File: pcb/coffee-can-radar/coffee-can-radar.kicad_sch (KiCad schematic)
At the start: 23 parts

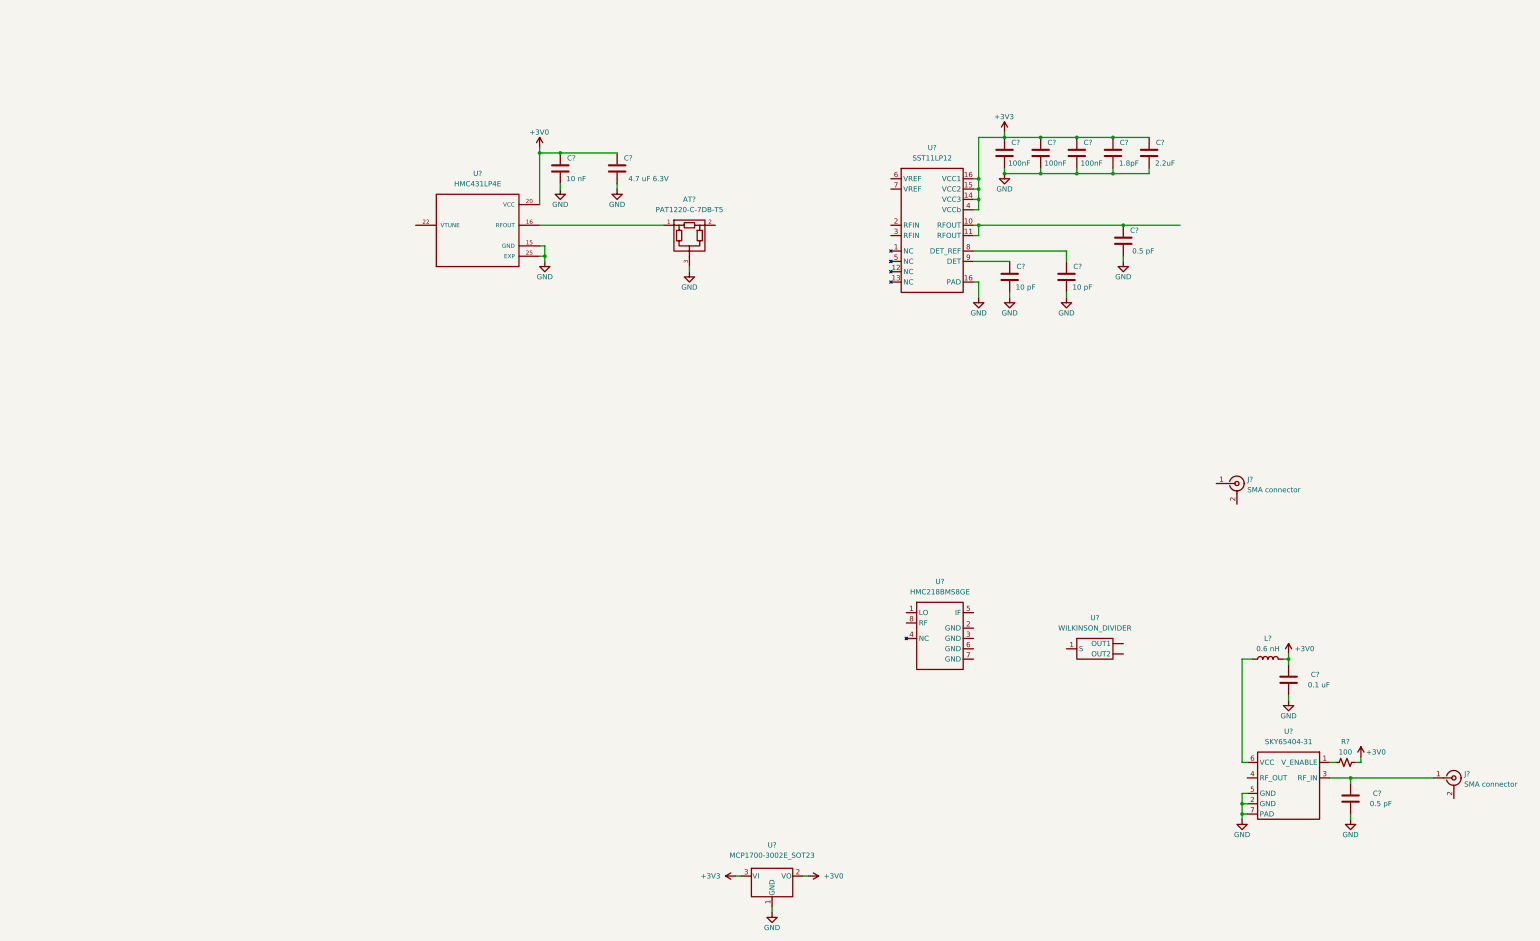
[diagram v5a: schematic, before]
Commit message: Finish RF, add supplies
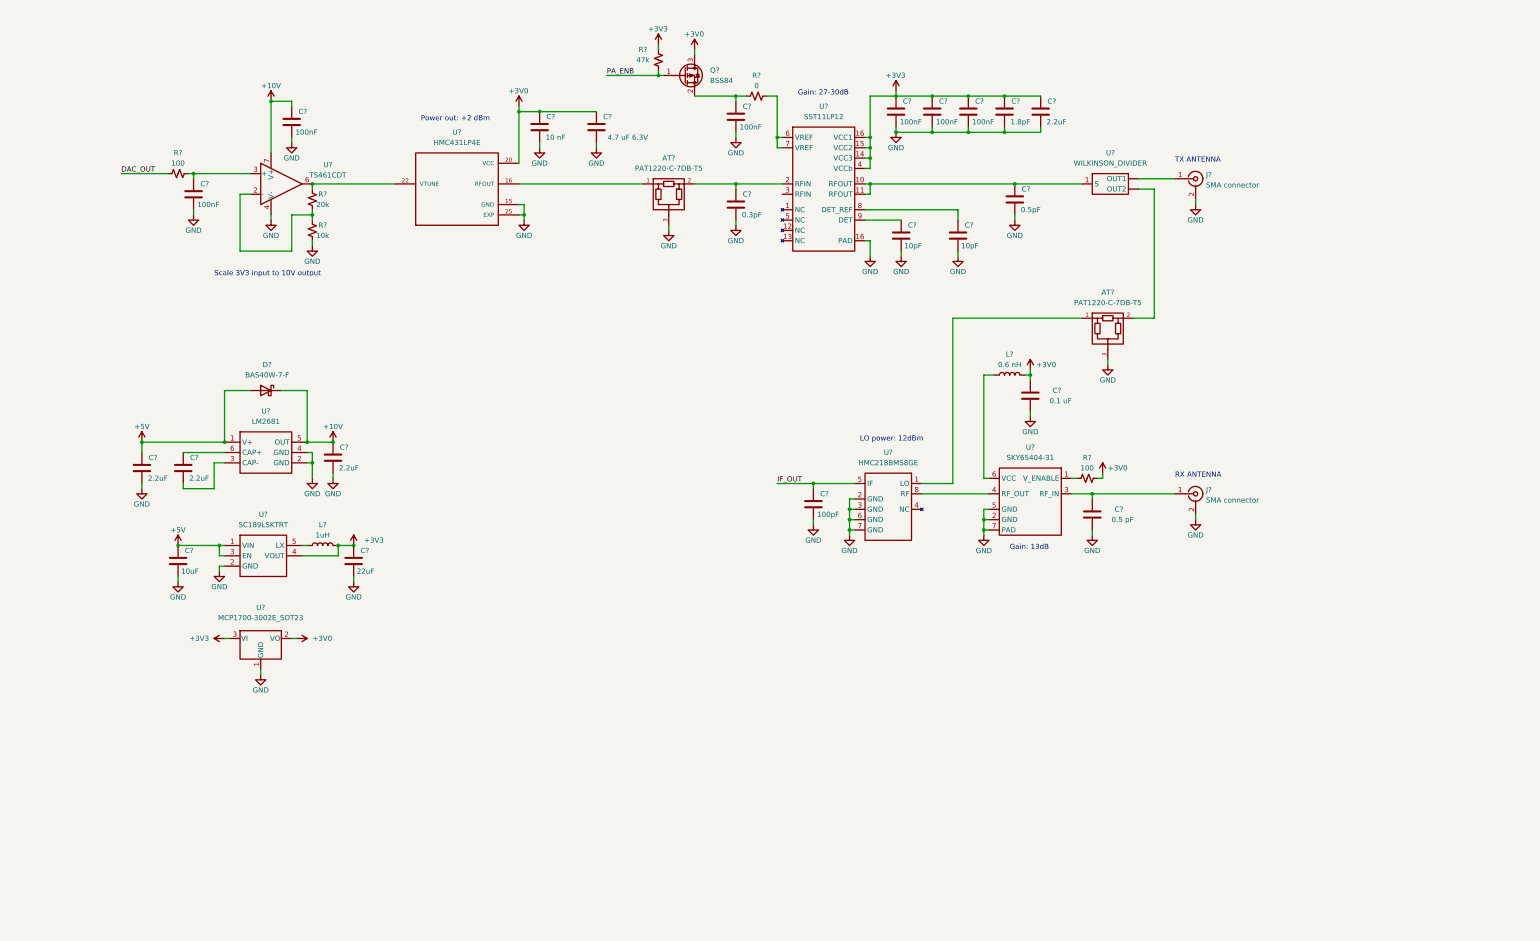
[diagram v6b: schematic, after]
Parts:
- added AT?: PAT1220-C-7DB-T5, ccr-footprints:ATTN_PAT1220-C-1DB-T5, symbol ccr-library:PAT1220-C-1DB-T5
- added C? (x3): 2.2uF, Capacitor_SMD:C_0603_1608Metric, symbol Device:C
- added C?: 10uF, Capacitor_SMD:C_0805_2012Metric, symbol Device:C
- added C? (x3): 100nF, Capacitor_SMD:C_0402_1005Metric, symbol Device:C
- added C?: 100pF, Capacitor_SMD:C_0402_1005Metric, symbol Device:C
- added C?: 22uF, Capacitor_SMD:C_0805_2012Metric, symbol Device:C
- added C?: 0.3pF, Capacitor_SMD:C_0402_1005Metric, symbol Device:C
- added D?: BAS40W-7-F, Package_TO_SOT_SMD:SOT-323_SC-70, symbol Device:D_Schottky
- added L?: 1uH, Inductor_SMD:L_1008_2520Metric, symbol Device:L
- added Q?: BSS84, Package_TO_SOT_SMD:SOT-23, symbol Transistor_FET:BSS84
- added R?: 10k, Resistor_SMD:R_0402_1005Metric, symbol Device:R_Small_US
- added R?: 20k, Resistor_SMD:R_0402_1005Metric, symbol Device:R_Small_US
- added R?: 47k, Resistor_SMD:R_0402_1005Metric, symbol Device:R_Small_US
- added R?: 100, Resistor_SMD:R_0402_1005Metric, symbol Device:R_Small_US
- added R?: 0, Resistor_SMD:R_0402_1005Metric, symbol Device:R_Small_US
- added U?: TS461CDT, Package_SO:SOIC-8-1EP_3.9x4.9mm_P1.27mm_EP2.29x3mm, symbol ccr-library:TS461CDT
- added U?: LM2681, Package_TO_SOT_SMD:SOT-23-6, symbol ccr-library:LM2681
- added U?: SC189LSKTRT, Package_TO_SOT_SMD:SOT-23-5, symbol ccr-library:SC189LSKTRT
- C?: value 0.5 pF -> 0.5pF
- C? (x2): value 10 pF -> 10pF
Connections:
- net +3V0: now also Q?.3 (D)
- net +3V3: now also C?.1, L?.2, R?.2, U?.4 (VOUT)
- net GND: now also J?.2 (Ext), J?.2 (Ext), U?.2 (GND), U?.3 (GND), U?.6 (GND), U?.7 (GND), AT?.3, C?.2, C?.2, C?.2, C?.2, C?.2, C?.2, C?.2, C?.2, C?.2, R?.2, U?.2 (GND), U?.2 (GND), U?.4 (GND), U?.4 (V-)
- net at C?.1, U?.10 (RFOUT), U?.11 (RFOUT): now also U?.1 (S)
- net at AT?.2: now also U?.2 (RFIN), C?.1
- net at U?.4 (RF_OUT): now also U?.8 (RF)
- net at U?.6 (VREF): now also U?.7 (VREF), R?.2
- net at U?.22 (VTUNE): now also R?.1, U?.6
- net at J?.1 (In): now also U?. (OUT2)
- net at U?.1 (LO): now also AT?.1
- net IF_OUT: now reaches U?.5 (IF)
- net IF_OUT: now also C?.1
- net at U?. (OUT2): now also AT?.2
- new net: R?.1, R?.2, U?.2 (-)
- new net: C?.1, R?.2, U?.3 (+)
- new net: C?.2, U?.3 (CAP-)
- new net: C?.1, U?.6 (CAP+)
- new net: L?.1, U?.5 (LX)
- new net: C?.1, Q?.2 (S), R?.1
- new net +10V: C?.1, C?.1, D?.1 (K), U?.5 (OUT), U?.7 (V+)
- new net +5V: C?.1, C?.1, D?.2 (A), U?.1 (V+), U?.1 (VIN), U?.3 (EN)
- new net DAC_OUT: R?.1
- new net PA_ENB: Q?.1 (G), R?.1
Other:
- note added: "Gain: 13dB"
- note added: "Gain: 27-30dB"
- note added: "LO power: 12dBm"
- note added: "Power out: +2 dBm"
- note added: "RX ANTENNA"
- note added: "Scale 3V3 input to 10V output"
- note added: "TX ANTENNA"
- moved on the sheet: AT?, C?, J?, L?, R?, U?

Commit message: Tidy up schematic
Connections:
- net IF_OUT renamed IF
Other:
- moved on the sheet: AT?, C?, D?, J?, L?, Q?, R?, U?

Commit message: Add header
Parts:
- added J?: Conn_01x04_Male, Connector_PinHeader_2.54mm:PinHeader_1x04_P2.54mm_Vertical, symbol Connector:Conn_01x04_Male
- added J?: SMA connector, symbol ccr-library:SMA connector
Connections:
- net +5V: now also J?.1 (Pin_1)
- net DAC_OUT: now also J?.3 (Pin_3)
- net GND: now also J?.4 (Pin_4)
- net IF: now also J?.1 (In)
- net PA_ENB: now also J?.2 (Pin_2)
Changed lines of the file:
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@@
+    (stroke (width 0) (type default) (color 0 0 0 0))
+  )
+  (wire (pts (xy 48.26 134.62) (xy 48.26 135.89))
     (stroke (width 0) (type default) (color 0 0 0 0))
   )
@@
     (stroke (width 0) (type default) (color 0 0 0 0))
   )
+  (wire (pts (xy 48.26 127) (xy 48.26 125.73))
+    (stroke (width 0) (type default) (color 0 0 0 0))
+  )
   (wire (pts (xy 146.05 49.53) (xy 146.05 36.83))
     (stroke (width 0) (type default) (color 0 0 0 0))
@@
     (stroke (width 0) (type default) (color 0 0 0 0))
   )
+  (wire (pts (xy 48.26 132.08) (xy 46.99 132.08))
+    (stroke (width 0) (type default) (color 0 0 0 0))
+  )
   (wire (pts (xy 321.31 142.24) (xy 322.58 142.24))
     (stroke (width 0) (type default) (color 0 0 0 0))
@@
     (stroke (width 0) (type default) (color 0 0 0 0))
   )
-  (wire (pts (xy 270.51 130.81) (xy 279.4 130.81))
+  (wire (pts (xy 269.24 130.81) (xy 279.4 130.81))
     (stroke (width 0) (type default) (color 0 0 0 0))
   )
@@
     (stroke (width 0) (type default) (color 0 0 0 0))
   )
+  (wire (pts (xy 48.26 129.54) (xy 46.99 129.54))
+    (stroke (width 0) (type default) (color 0 0 0 0))
+  )
   (wire (pts (xy 292.1 50.8) (xy 293.37 50.8))
     (stroke (width 0) (type default) (color 0 0 0 0))
@@
     (stroke (width 0) (type default) (color 0 0 0 0))
   )
+  (wire (pts (xy 46.99 127) (xy 48.26 127))
+    (stroke (width 0) (type default) (color 0 0 0 0))
+  )
   (wire (pts (xy 288.29 137.16) (xy 289.56 137.16))
     (stroke (width 0) (type default) (color 0 0 0 0))
@@
   )
   (wire (pts (xy 48.26 68.58) (xy 48.26 66.04))
+    (stroke (width 0) (type default) (color 0 0 0 0))
+  )
+  (wire (pts (xy 46.99 134.62) (xy 48.26 134.62))
     (stroke (width 0) (type default) (color 0 0 0 0))
   )
@@
     (effects (font (size 1.27 1.27)) (justify left bottom))
   )
+  (label "DAC_OUT" (at 48.26 132.08 0)
+    (effects (font (size 1.27 1.27)) (justify left bottom))
+  )
   (label "PA_ENB" (at 228.6 30.48 0)
     (effects (font (size 1.27 1.27)) (justify left bottom))
@@
     (effects (font (size 1.27 1.27)) (justify left bottom))
   )
+  (label "PA_ENB" (at 48.26 129.54 0)
+    (effects (font (size 1.27 1.27)) (justify left bottom))
+  )
   (label "DAC_OUT" (at 109.22 54.61 0)
     (effects (font (size 1.27 1.27)) (justify left bottom))
@@
     (pin "1")
     (pin "2")
+  )
+  (symbol (lib_id "Connector:Conn_01x04_Male") (at 41.91 129.54 0) (unit 1)
+    (in_bom yes) (on_board yes)
+    (property "Reference" "J?" (id 0) (at 42.545 121.92 0))
+    (property "Value" "Conn_01x04_Male" (id 1) (at 49.53 119.38 0))
+    (property "Footprint" "Connector_PinHeader_2.54mm:PinHeader_1x04_P2.54mm_Vertical" (id 2) (at 41.91 129.54 0)
+      (effects (font (size 1.27 1.27)) hide)
+    )
+    (property "Datasheet" "~" (id 3) (at 41.91 129.54 0)
+      (effects (font (size 1.27 1.27)) hide)
+    )
+    (pin "1")
+    (pin "2")
+    (pin "3")
+    (pin "4")
   )
   (symbol (lib_id "power:GND") (at 76.2 49.53 0) (unit 1)
@@
     (pin "1")
   )
+  (symbol (lib_id "power:GND") (at 48.26 135.89 0) (unit 1)
+    (in_bom yes) (on_board yes)
+    (property "Reference" "#PWR?" (id 0) (at 48.26 142.24 0)
+      (effects (font (size 1.27 1.27)) hide)
+    )
+    (property "Value" "GND" (id 1) (at 48.26 139.7 0))
+    (property "Footprint" "" (id 2) (at 48.26 135.89 0)
+      (effects (font (size 1.27 1.27)) hide)
+    )
+    (property "Datasheet" "" (id 3) (at 48.26 135.89 0)
+      (effects (font (size 1.27 1.27)) hide)
+    )
+    (pin "1")
+  )
   (symbol (lib_id "Device:C") (at 39.37 46.99 0) (mirror y) (unit 1)
     (in_bom yes) (on_board yes)
@@
     (pin "3")
   )
+  (symbol (lib_id "power:+5V") (at 48.26 125.73 0) (unit 1)
+    (in_bom yes) (on_board yes)
+    (property "Reference" "#PWR?" (id 0) (at 48.26 129.54 0)
+      (effects (font (size 1.27 1.27)) hide)
+    )
+    (property "Value" "+5V" (id 1) (at 48.26 121.92 0))
+    (property "Footprint" "" (id 2) (at 48.26 125.73 0)
+      (effects (font (size 1.27 1.27)) hide)
+    )
+    (property "Datasheet" "" (id 3) (at 48.26 125.73 0)
+      (effects (font (size 1.27 1.27)) hide)
+    )
+    (pin "1")
+  )
   (symbol (lib_id "Device:C") (at 300.99 69.85 0) (mirror y) (unit 1)
     (in_bom yes) (on_board yes)
@@
     )
     (pin "1")
+  )
+  (symbol (lib_id "ccr-library:SMA connector") (at 264.16 130.81 0) (mirror y) (unit 1)
+    (in_bom yes) (on_board yes) (fields_autoplaced)
+    (property "Reference" "J?" (id 0) (at 264.4774 123.19 0))
+    (property "Value" "SMA connector" (id 1) (at 264.4774 125.73 0))
+    (property "Footprint" "" (id 2) (at 264.16 130.81 0)
+      (effects (font (size 1.27 1.27)) hide)
+    )
+    (property "Datasheet" " ~" (id 3) (at 264.16 130.81 0)
+      (effects (font (size 1.27 1.27)) hide)
+    )
+    (pin "1")
+    (pin "2")
   )
   (symbol (lib_id "Device:C") (at 279.4 135.89 0) (mirror y) (unit 1)
@@
       (reference "#PWR?") (unit 1) (value "+5V") (footprint "")
     )
+    (path "/6521881a-1f2f-4029-8ce1-c88860d10c74"
+      (reference "#PWR?") (unit 1) (value "GND") (footprint "")
+    )
     (path "/7c27d919-e5cd-4d50-b031-4ff3eb595757"
       (reference "#PWR?") (unit 1) (value "GND") (footprint "")
@@
       (reference "#PWR?") (unit 1) (value "+3V0") (footprint "")
     )
+    (path "/882a6564-c5df-4657-a77c-8fdd6234cd4b"
+      (reference "#PWR?") (unit 1) (value "+5V") (footprint "")
+    )
     (path "/919a3675-581a-4846-a6be-42ea46241e38"
       (reference "#PWR?") (unit 1) (value "GND") (footprint "")
@@
       (reference "D?") (unit 1) (value "BAS40W-7-F") (footprint "Package_TO_SOT_SMD:SOT-323_SC-70")
     )
+    (path "/0802a44c-b7d1-4d00-83de-b654b649779a"
+      (reference "J?") (unit 1) (value "Conn_01x04_Male") (footprint "Connector_PinHeader_2.54mm:PinHeader_1x04_P2.54mm_Vertical")
+    )
     (path "/5f968713-62b6-4aff-8649-2fe586ca1b69"
       (reference "J?") (unit 1) (value "SMA connector") (footprint "")
     )
+    (path "/b936823f-ca1a-4f54-965e-9057628ed24f"
+      (reference "J?") (unit 1) (value "SMA connector") (footprint "")
+    )
